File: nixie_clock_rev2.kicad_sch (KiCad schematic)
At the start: 0 parts

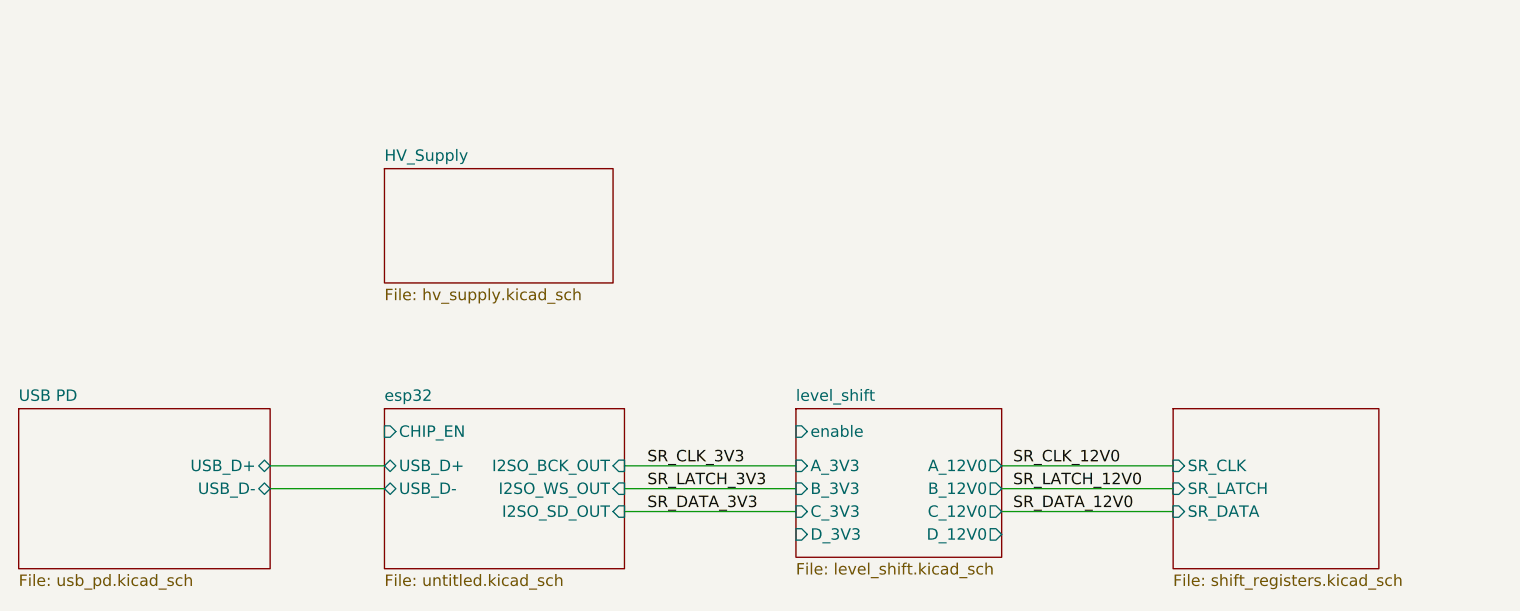
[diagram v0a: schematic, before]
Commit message: built out power supplies, added datasheets
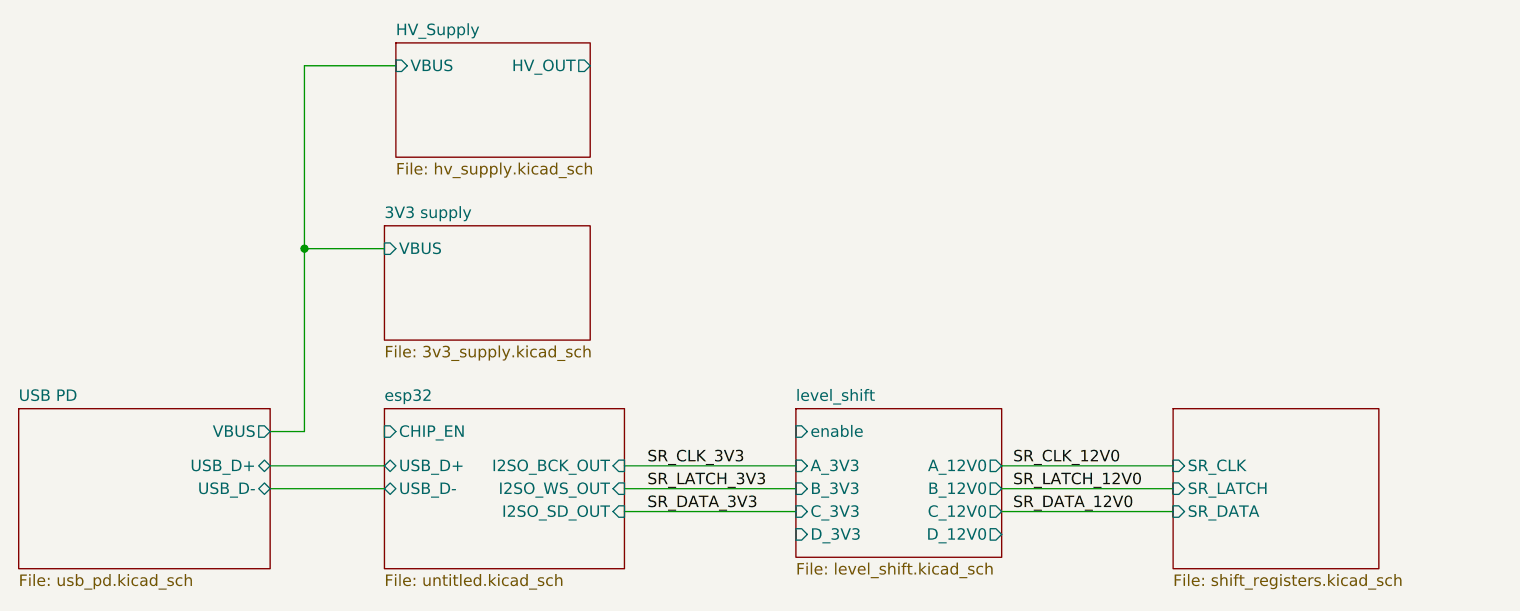
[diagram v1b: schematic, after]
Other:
- added sheet 3V3 supply (3v3_supply.kicad_sch)
- sheet HV_Supply ports: added HV_OUT, VBUS; removed none
- sheet USB PD ports: added VBUS; removed none
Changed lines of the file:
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@@
 (kicad_sch (version 20230121) (generator eeschema)
   (paper "USLetter")
+  (junction (at 86.36 63.5) (diameter 0) (color 0 0 0 0)
+  )
   (wire (pts (xy 82.55 90.17) (xy 95.25 90.17))
     (stroke (width 0) (type default))
   )
+  (wire (pts (xy 86.36 63.5) (xy 95.25 63.5))
+    (stroke (width 0) (type default))
+  )
   (wire (pts (xy 163.83 92.71) (xy 182.88 92.71))
     (stroke (width 0) (type default))
   )
+  (wire (pts (xy 96.52 43.18) (xy 86.36 43.18))
+    (stroke (width 0) (type default))
+  )
   (wire (pts (xy 121.92 90.17) (xy 140.97 90.17))
     (stroke (width 0) (type default))
@@
     (stroke (width 0) (type default))
   )
+  (wire (pts (xy 82.55 83.82) (xy 86.36 83.82))
+    (stroke (width 0) (type default))
+  )
+  (wire (pts (xy 86.36 43.18) (xy 86.36 63.5))
+    (stroke (width 0) (type default))
+  )
   (wire (pts (xy 163.83 90.17) (xy 182.88 90.17))
     (stroke (width 0) (type default))
@@
     (stroke (width 0) (type default))
   )
+  (wire (pts (xy 86.36 83.82) (xy 86.36 63.5))
+    (stroke (width 0) (type default))
+  )
   (wire (pts (xy 82.55 87.63) (xy 95.25 87.63))
     (stroke (width 0) (type default))
@@
       (project "nixie_clock_rev2"
         (path "/0fc2f476-9e20-4198-a623-ece581a79a9a" (page "3"))
+      )
+    )
+  )
+  (sheet (at 95.25 60.96) (size 22.86 12.7) (fields_autoplaced)
+    (stroke (width 0.1524) (type solid))
+    (fill (color 0 0 0 0.0000))
+    (property "Sheetname" "3V3 supply" (at 95.25 60.2484 0)
+      (effects (font (size 1.27 1.27)) (justify left bottom))
+    )
+    (property "Sheetfile" "3v3_supply.kicad_sch" (at 95.25 74.2446 0)
+      (effects (font (size 1.27 1.27)) (justify left top))
+    )
+    (property "Field2" "" (at 95.25 60.96 0)
+      (effects (font (size 1.27 1.27)) hide)
+    )
+    (pin "VBUS" input (at 95.25 63.5 180)
+      (effects (font (size 1.27 1.27)) (justify left))
+    )
+    (instances
+      (project "nixie_clock_rev2"
+        (path "/0fc2f476-9e20-4198-a623-ece581a79a9a" (page "10"))
       )
     )
@@
     )
   )
-  (sheet (at 95.25 54.61) (size 25.4 12.7) (fields_autoplaced)
-    (stroke (width 0.1524) (type solid))
-    (fill (color 0 0 0 0.0000))
-    (property "Sheetname" "HV_Supply" (at 95.25 53.8984 0)
-      (effects (font (size 1.27 1.27)) (justify left bottom))
-    )
-    (property "Sheetfile" "hv_supply.kicad_sch" (at 95.25 67.8946 0)
-      (effects (font (size 1.27 1.27)) (justify left top))
+  (sheet (at 96.52 40.64) (size 21.59 12.7) (fields_autoplaced)
+    (stroke (width 0.1524) (type solid))
+    (fill (color 0 0 0 0.0000))
+    (property "Sheetname" "HV_Supply" (at 96.52 39.9284 0)
+      (effects (font (size 1.27 1.27)) (justify left bottom))
+    )
+    (property "Sheetfile" "hv_supply.kicad_sch" (at 96.52 53.9246 0)
+      (effects (font (size 1.27 1.27)) (justify left top))
+    )
+    (pin "VBUS" input (at 96.52 43.18 180)
+      (effects (font (size 1.27 1.27)) (justify left))
+    )
+    (pin "HV_OUT" output (at 118.11 43.18 0)
+      (effects (font (size 1.27 1.27)) (justify right))
     )
     (instances
@@
       (effects (font (size 1.27 1.27)) (justify right))
     )
+    (pin "VBUS" output (at 82.55 83.82 0)
+      (effects (font (size 1.27 1.27)) (justify right))
+    )

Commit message: added fet-based level shifter
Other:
- sheet level_shift ports: added none; removed enable
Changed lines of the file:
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@@
-      (effects (font (size 1.27 1.27)) (justify left))
-    )
-    (pin "enable" input (at 140.97 83.82 180)
       (effects (font (size 1.27 1.27)) (justify left))
     )
